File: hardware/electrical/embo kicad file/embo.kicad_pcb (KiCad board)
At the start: 2 copper layers, 96.4 x 46.6 mm, 109 parts, among them IC1 OPA2354, IC2 OPA2354, J1 Conn_Coaxial, J13 USB_C_Receptacle_USB2.0_16P, J14 24 V PSU input, J2 Conn_Coaxial, J3 UART to RPi, J4 JSTXH 6pin Socket 1, J5 JSTXH 6pin Socket 2, J6 motor 1, J7 motor 2, J8 LED Panel, J9 Conn_02x10_Odd_Even, Q1 AO4407A, U1 ESP32-S3-WROOM-1, U2 LM2596S-5, U3 AMS1117-3.3, U4 AD9833xRM, U5 TMC2209-LA, U6 TMC2209-LA

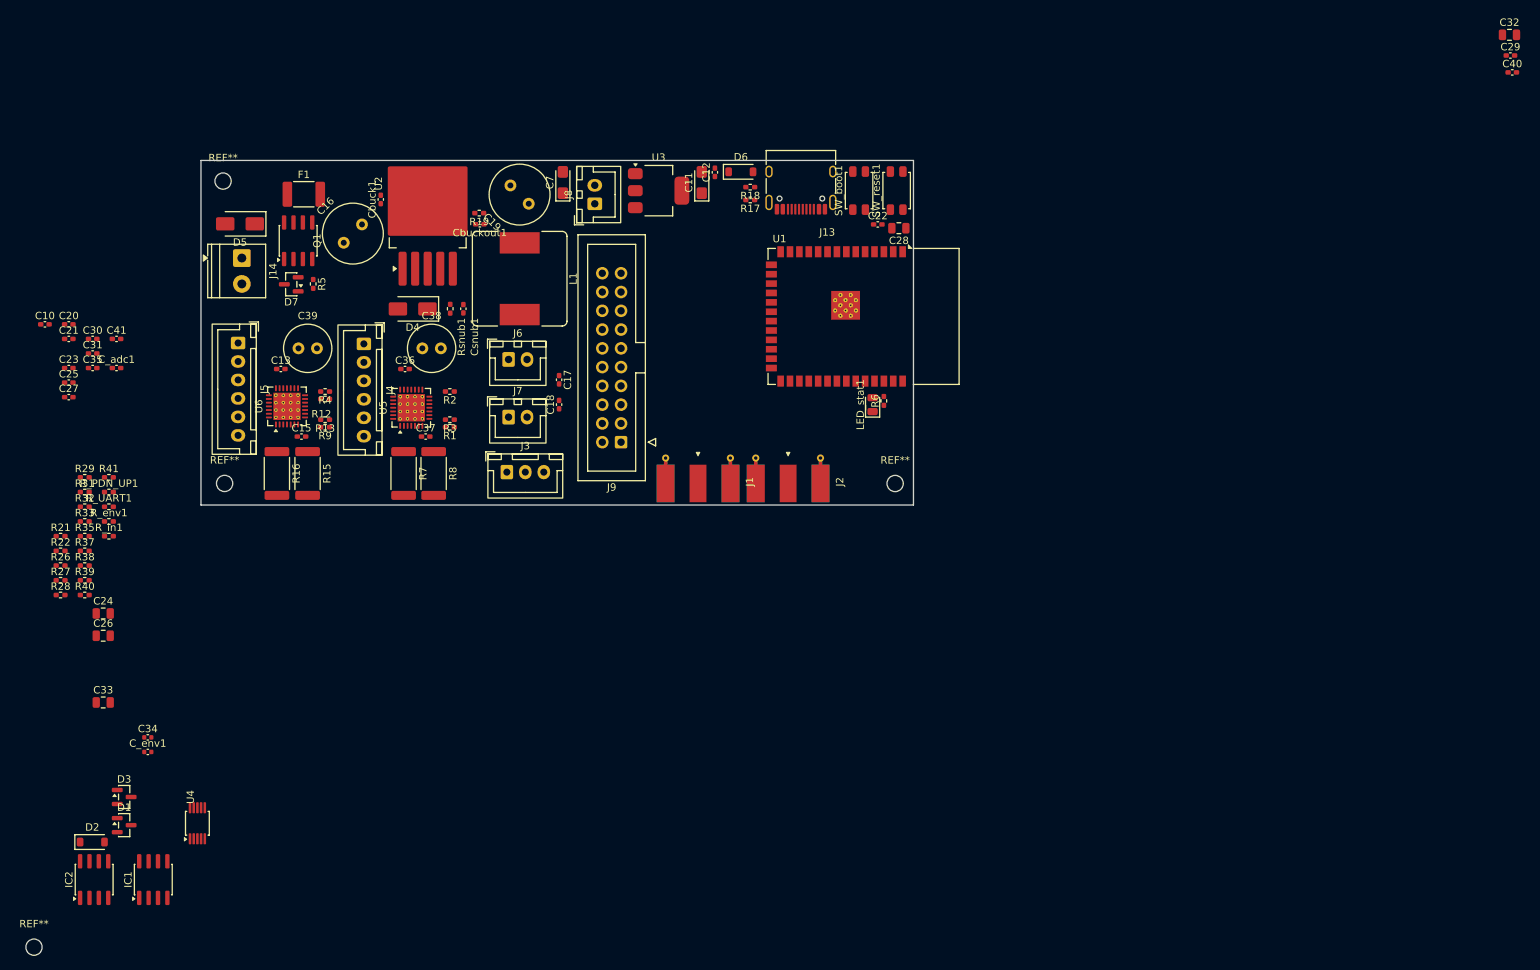
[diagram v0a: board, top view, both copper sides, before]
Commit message: main PCB layout update
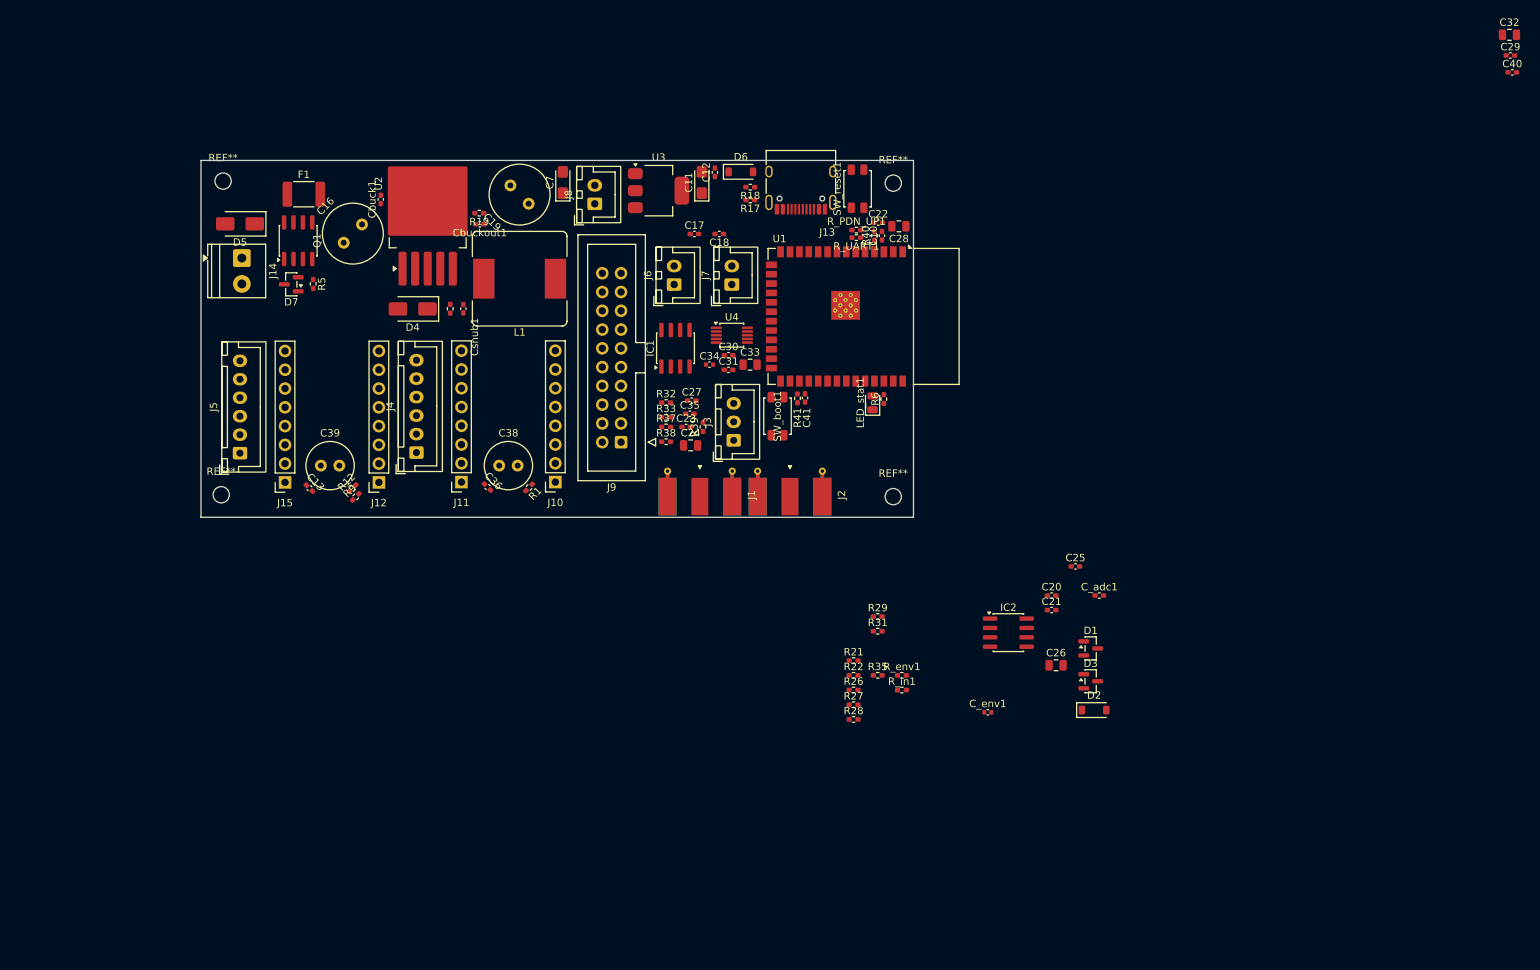
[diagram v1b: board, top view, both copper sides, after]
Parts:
- removed C15, C37: 100nF X7R, Capacitor_SMD:C_0402_1005Metric_Pad0.74x0.62mm_HandSolder
- removed R13, R2, R3, R4: 10kΩ, Resistor_SMD:R_0402_1005Metric_Pad0.72x0.64mm_HandSolder
- removed R15, R16, R7, R8: 0.11Ω, Resistor_SMD:R_2512_6332Metric
- removed U5, U6: TMC2209-LA, Package_DFN_QFN:VQFN-28-1EP_5x5mm_P0.5mm_EP3.7x3.7mm_ThermalVias
- added J10: Conn_01x08, Connector_PinSocket_2.54mm:PinSocket_1x08_P2.54mm_Vertical, F.Cu at (144.5, 114.1)
- added J11: Conn_01x08, Connector_PinSocket_2.54mm:PinSocket_1x08_P2.54mm_Vertical, F.Cu at (131.8, 114.1)
- added J12: Conn_01x08, Connector_PinSocket_2.54mm:PinSocket_1x08_P2.54mm_Vertical, F.Cu at (120.7, 114.2)
- added J15: Conn_01x08, Connector_PinSocket_2.54mm:PinSocket_1x08_P2.54mm_Vertical, F.Cu at (108.0, 114.2)
- C38, C39: footprint Capacitor_THT:C_Radial_D6.3mm_H11.0mm_P2.50mm -> Capacitor_THT:C_Radial_D6.3mm_H7.0mm_P2.50mm
- moved REF** 155.6 mm to (190.2, 73.7)
- moved C25 138.5 mm to (214.9, 125.5)
- moved C20 137.9 mm to (211.7, 129.5)
- moved C21 137.9 mm to (211.7, 131.4)
- moved D2 136.7 mm to (217.4, 145.0)
- moved C_adc1 136.5 mm to (218.1, 129.5)
- moved D1 132.9 mm to (217.0, 136.6)
- moved D3 131.7 mm to (217.0, 141.1)
- moved C26 129.0 mm to (212.3, 138.9)
- moved IC2 128.1 mm to (205.8, 134.5), turned to 0 degrees
- moved R40 117.4 mm to (187.7, 80.8), turned to 90 degrees
- moved C10 113.9 mm to (188.7, 80.8), turned to 90 degrees
- moved C_env1 113.8 mm to (203.0, 145.3)
- moved R_env1 109.3 mm to (191.4, 140.3)
- moved R_in1 109.3 mm to (191.4, 142.2)
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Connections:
- J4 pad 1: /M1_A1 -> /M1_A2
- J4 pad 3: /M1_A2 -> /M1_A1
- J5 pad 1: /M2_A1 -> /M2_A2
- J5 pad 3: /M2_A2 -> /M2_A1
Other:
- board size 96.4 x 46.6 mm -> 96.4 x 48.3 mm
